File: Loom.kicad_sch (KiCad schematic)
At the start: 49 parts

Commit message: more updates to power distribution
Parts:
- removed FBX1, FBX2: Conn_01x10, symbol Connector_Generic:Conn_01x10
- added FBX1, FBX2: Conn_01x16, symbol Connector_Generic:Conn_01x16
- added PBX1, PBX2: Conn_01x19, symbol Connector_Generic:Conn_01x19
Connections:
- net FPSig: now also PBX2.2 (Pin_2); no longer ECU.8 (Pin_8)
- net FanSig: now also PBX2.4 (Pin_4)
- net GND: now also WSR.8 (Pin_8)
- net MiscPWR: now also FBX1.6 (Pin_6), PBX2.13 (Pin_13); no longer RBX4.85, RBX5.85
- net SENGND: no longer WSR.8 (Pin_8)
- net Shutdown: now also PBX2.1 (Pin_1); no longer LES.2 (Pin_2)
- net SparkCut: now also PBX2.3 (Pin_3)
- net at DBX.1 (Pin_1), DBX.2 (Pin_2), DBX.3 (Pin_3)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: now also FBX2.1 (Pin_1), FBX2.2 (Pin_2), FBX2.3 (Pin_3), FBX2.4 (Pin_4), FBX2.5 (Pin_5), FBX2.6 (Pin_6), FBX2.7 (Pin_7), FBX2.8 (Pin_8)
- net at RBX1.30: now also FBX2.12 (Pin_12), FBX2.13 (Pin_13)
- net at RBX2.30: now also FBX2.14 (Pin_14)
- net at RBX4.30: now also FBX2.15 (Pin_15)
- net at RBX5.30: now also FBX2.16 (Pin_16)
- net FPPWR: no longer names the net of FLP.1 (Pin_1)
- net FanPWR: no longer names the net of FAN1.1 (Pin_1), FAN2.1 (Pin_1)
- net QSPWR renamed QS_12V
- net SPKPWR renamed SpkPwr
- new net: LES.2 (Pin_2), PBX1.1 (Pin_1)
- new net BrakeLightPwr: FBX1.7 (Pin_7), PBX2.15 (Pin_15)
- new net ECUPwr: FBX1.1 (Pin_1), PBX2.5 (Pin_5)
- new net ETCCUPwr: FBX1.3 (Pin_3), PBX2.7 (Pin_7)
- new net ETCStepPwr: FBX1.4 (Pin_4), PBX2.9 (Pin_9)
- new net FPPwr: FBX1.14 (Pin_14), PBX2.10 (Pin_10)
- new net FanPwr: FBX1.16 (Pin_16), PBX2.14 (Pin_14)
- new net INJAPwr: FBX1.12 (Pin_12), PBX2.17 (Pin_17)
- new net INJBPwr: FBX1.13 (Pin_13), PBX2.19 (Pin_19)
- new net LambdaPwr: FBX1.2 (Pin_2), PBX2.6 (Pin_6)
- new net MiscPwr: FBX1.8 (Pin_8), PBX2.8 (Pin_8)
- new net ShutdownPwr: FBX1.5 (Pin_5), PBX2.11 (Pin_11), RBX4.85, RBX5.85
- new net SparkPwr: FBX1.15 (Pin_15), PBX2.12 (Pin_12)
- no-connect marks 10 -> 19
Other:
- sheet Front of Firewall ports: added Brake Light Power, ETC CU Power, Shutdown Power; removed none
- note added: "ECU 2A Lambda 5A ETC CU 5A ETC Stepper 5A Shutdown 5A QS CU 5A Brake Light 5A Misc 10A INJA 5A INJB 5A FP 10A Spark 20A Fans 20A"
- note added: "FIREWALL CONNECTOR HDP24-24-31SE Pinout: 1 MiscPWR 2 ETC CU Power 3 StepperPWR 4 IdleCtrl 5 Blip 6 TPS Power 1 7 TPS Signal 1 8 TPS Ground 1 9 TPS Power 2 10 TPS Signal 2 11 TPS Ground 2 12 Stepper 1+ 13 Stepper 1- 14 Stepper 2+ 15 Stepper 2- 16 Neutral 17 Shift Down 18 Shift Up 19 Tachometer 20 Shutdown Out 21 Starter Sig 22 Fan Sig 23 BLS Sig 24 Launch Sig 25 Launch LED 26 27 28 Brake Light PWR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"
- note added: "Red - up to 15A each Green - up to 20A each"
- note removed: "ECU 2A Lambda 5A ETC CU 5A ETC Stepper 5A Shutdown Circuit 5A QS CU 5A Brake Light 5A Supplemental Electronics 10A INJA 5A INJB 5A FP 10A Spark 20A Fans 20A"
- note removed: "FIREWALL CONNECTOR HDP24-24-31SE Pinout: 1 MiscPWR 2 StepperPWR 3 4 IdleCtrl 5 Blip 6 TPS Power 1 7 TPS Signal 1 8 TPS Ground 1 9 TPS Power 2 10 TPS Signal 2 11 TPS Ground 2 12 Stepper 1+ 13 Stepper 1- 14 Stepper 2+ 15 Stepper 2- 16 Neutral 17 Shift Down 18 Shift Up 19 Tachometer 20 Shutdown Out 21 Starter Sig 22 Fan Sig 23 BLS Sig 24 Launch Sig 25 Launch LED 26 27 28 29 CANH 30 CANL 31 SENGND"
- moved on the sheet: FAN1, FAN2

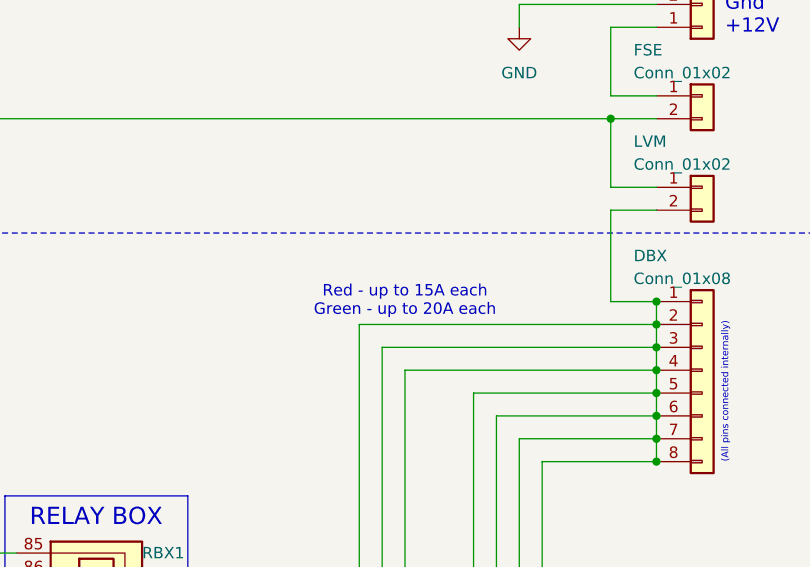
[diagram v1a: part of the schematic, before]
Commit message: More power distribution updates
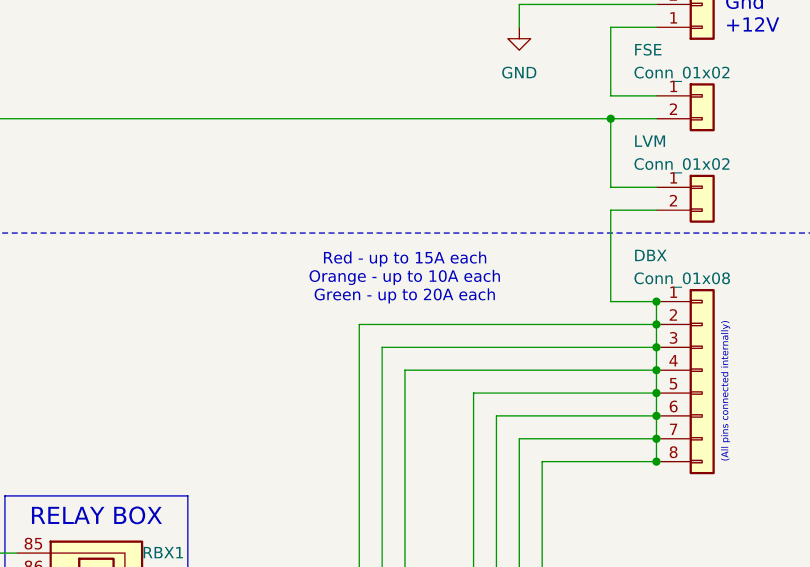
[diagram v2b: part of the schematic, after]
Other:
- note added: "Red - up to 15A each Orange - up to 10A each Green - up to 20A each"
- note removed: "Red - up to 15A each Green - up to 20A each"
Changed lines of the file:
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@@
 		)
 	)
-	(text "Red - up to 15A each\nGreen - up to 20A each"
+	(text "Red - up to 15A each\nOrange - up to 10A each\nGreen - up to 20A each"
 		(exclude_from_sim no)
-		(at 530.86 160.02 0)
+		(at 530.86 157.48 0)
 		(effects
 			(font
@@
 		(at 474.98 284.48)
 		(diameter 0)
-		(color 0 0 0 0)
+		(color 0 255 0 1)
 	)
 	(junction
@@
 		(at 485.14 251.46)
 		(diameter 0)
-		(color 0 0 0 0)
+		(color 0 255 0 1)
 	)
 	(junction
@@
 			(width 0)
 			(type default)
+			(color 0 255 0 1)
 		)
 	)
@@
 			(width 0)
 			(type default)
+			(color 0 255 0 1)
 		)
 	)
@@
 			(width 0)
 			(type default)
+			(color 226 113 0 1)
 		)
 	)
@@
 			(width 0)
 			(type default)
+			(color 0 255 0 1)
 		)
 	)
@@
 			(width 0)
 			(type default)
+			(color 0 255 0 1)
 		)
 	)
@@
 			(width 0)
 			(type default)
+			(color 0 255 0 1)
 		)
 	)
@@
 			(width 0)
 			(type default)
+			(color 0 255 0 1)
 		)
 	)
@@
 			(width 0)
 			(type default)
-			(color 255 0 0 1)
+			(color 0 255 0 1)
 		)
 	)
@@
 			(width 0)
 			(type default)
+			(color 226 113 0 1)
 		)
 	)
@@
 			(width 0)
 			(type default)
+			(color 0 255 0 1)
 		)
 	)
@@
 			(width 0)
 			(type default)
+			(color 0 255 0 1)
 		)
 	)
@@
 			(width 0)
 			(type default)
+			(color 0 255 0 1)
 		)
 	)
@@
 			(width 0)
 			(type default)
+			(color 0 255 0 1)
 		)
 	)
@@
 			(width 0)
 			(type default)
+			(color 226 113 0 1)
 		)
 	)
@@
 			(width 0)
 			(type default)
+			(color 226 113 0 1)
 		)
 	)
@@
 			(width 0)
 			(type default)
+			(color 0 255 0 1)
 		)
 	)
@@
 			(width 0)
 			(type default)
+			(color 0 255 0 1)
 		)
 	)
@@
 			(width 0)
 			(type default)
+			(color 0 255 0 1)
 		)
 	)
@@
 			(width 0)
 			(type default)
+			(color 0 255 0 1)
 		)
 	)
@@
 			(width 0)
 			(type default)
+			(color 0 255 0 1)
 		)
 	)
@@
 			(width 0)
 			(type default)
+			(color 0 255 0 1)
 		)
 	)
@@
 			(width 0)
 			(type default)
+			(color 0 255 0 1)
 		)
 	)
@@
 			(width 0)
 			(type default)
-			(color 255 0 0 1)
+			(color 0 255 0 1)
 		)
 	)
@@
 			(width 0)
 			(type default)
+			(color 0 255 0 1)
 		)
 	)
@@
 			(width 0)
 			(type default)
+			(color 0 255 0 1)
 		)
 	)
@@
 			(width 0)
 			(type default)
+			(color 0 255 0 1)
 		)
 	)
@@
 			(width 0)
 			(type default)
+			(color 0 255 0 1)
 		)
 	)
@@
 			(width 0)
 			(type default)
+			(color 0 255 0 1)
 		)
 	)
@@
 			(width 0)
 			(type default)
+			(color 0 255 0 1)
 		)
 	)
@@
 			(width 0)
 			(type default)
+			(color 0 255 0 1)
 		)
 	)
@@
 			(width 0)
 			(type default)
-			(color 255 0 0 1)
+			(color 0 255 0 1)
 		)
 	)
@@
 			(width 0)
 			(type default)
+			(color 0 255 0 1)
 		)
 	)
@@
 			(width 0)
 			(type default)
+			(color 226 113 0 1)
 		)
 	)
@@
 			(width 0)
 			(type default)
+			(color 0 255 0 1)
 		)
 	)
@@
 			(width 0)
 			(type default)
+			(color 0 255 0 1)
 		)
 	)
@@
 			(width 0)
 			(type default)
+			(color 0 255 0 1)
 		)
 	)
@@
 			(width 0)
 			(type default)
+			(color 226 113 0 1)
 		)
 	)
@@
 			(width 0)
 			(type default)
+			(color 0 255 0 1)
 		)
 	)
@@
 			(width 0)
 			(type default)
+			(color 0 255 0 1)
 		)
 	)
@@
 			(width 0)
 			(type default)
-			(color 255 0 0 1)
+			(color 0 255 0 1)
 		)
 	)
@@
 			(width 0)
 			(type default)
+			(color 0 255 0 1)
 		)
 	)
@@
 			(width 0)
 			(type default)
+			(color 0 255 0 1)
 		)
 	)
@@
 			(width 0)
 			(type default)
+			(color 0 255 0 1)
 		)
 	)

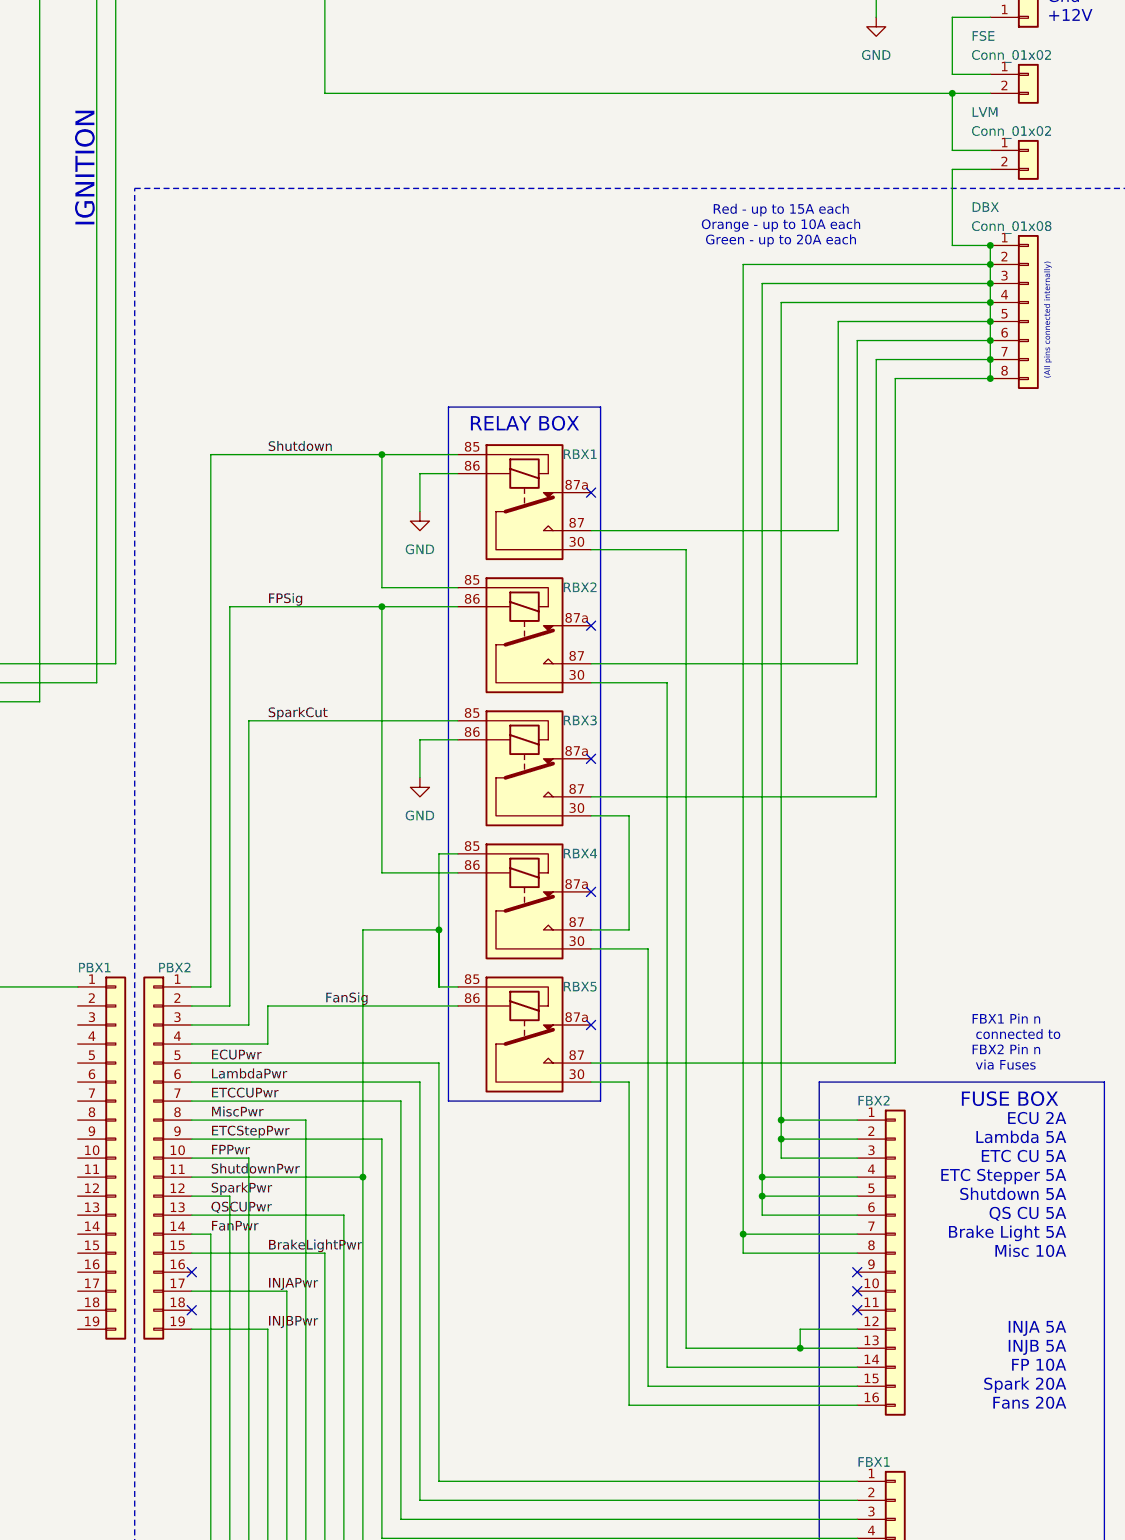
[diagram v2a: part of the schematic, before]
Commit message: Power Box Changes 20250714
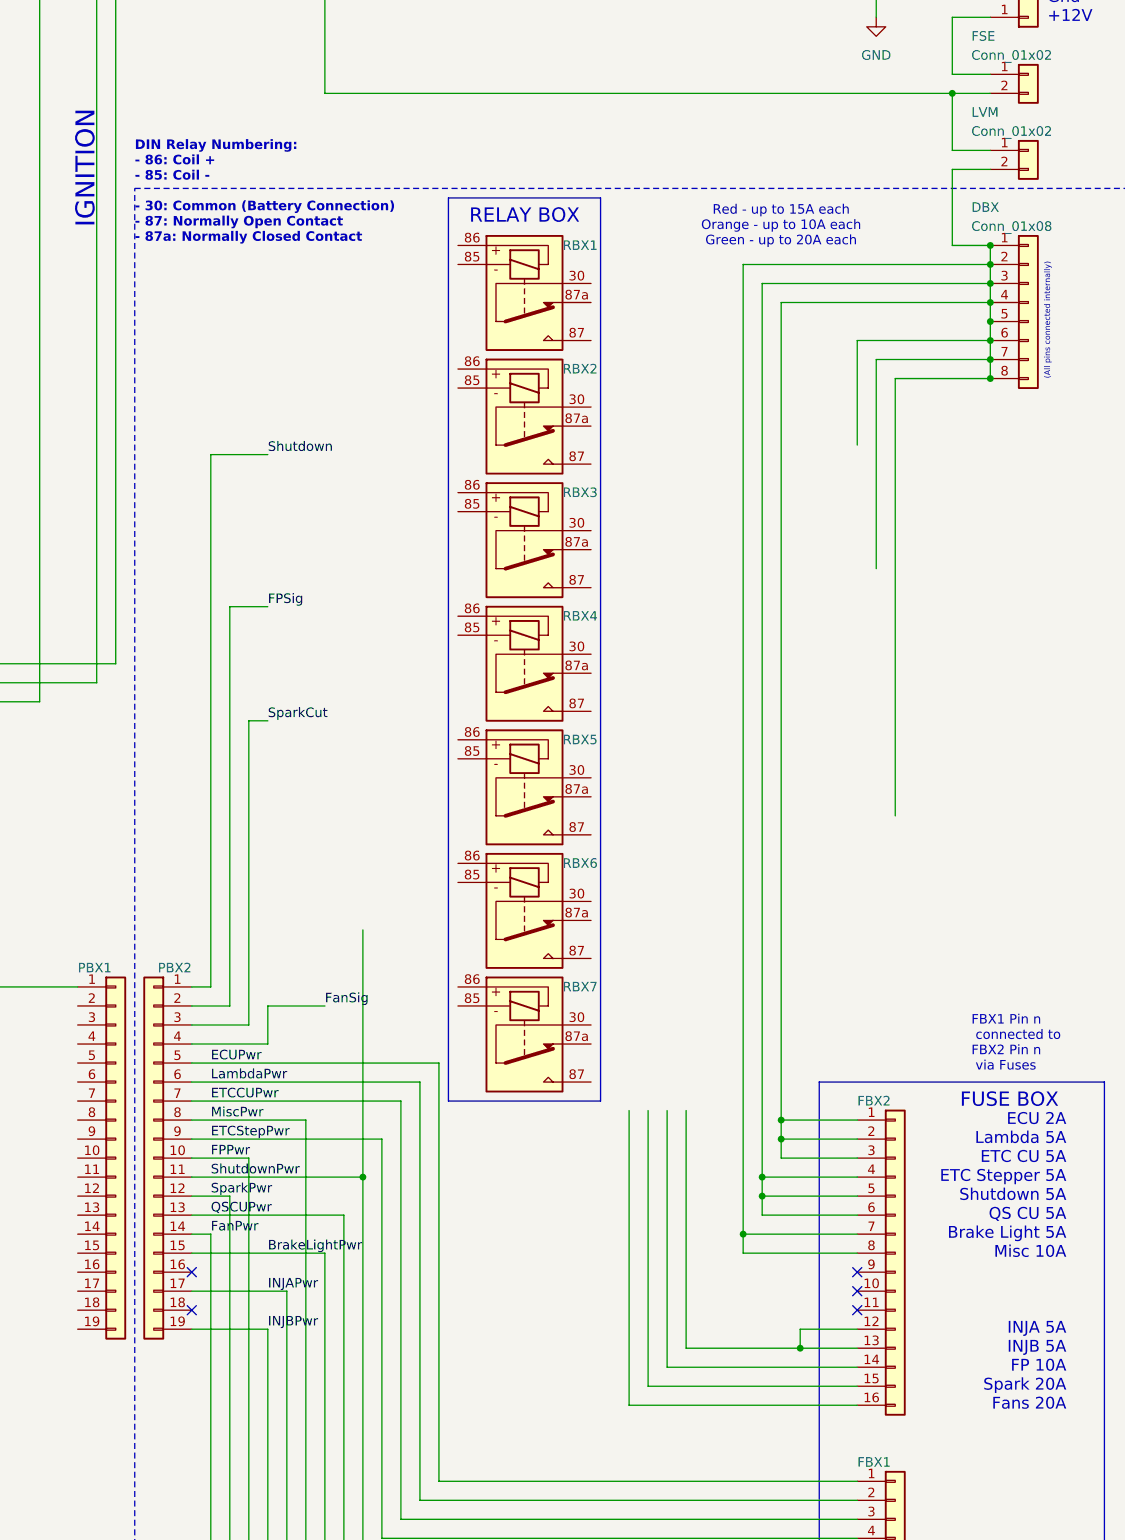
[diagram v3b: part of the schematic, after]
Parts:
- added RBX6, RBX7: Relay_SPDT_Automotive, symbol FBR_Symbols:Relay_SPDT_Automotive
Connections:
- net FPSig: no longer RBX2.86, RBX4.86
- net FanSig: no longer RBX5.86
- net GND: no longer RBX1.86, RBX3.86
- net Shutdown: no longer RBX1.85, RBX2.85
- net ShutdownPwr: no longer RBX4.85, RBX5.85
- net SparkCut: no longer RBX3.85
- net at DBX.1 (Pin_1), DBX.2 (Pin_2), DBX.3 (Pin_3)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: no longer RBX1.87, RBX2.87, RBX3.87, RBX5.87
- net at RBX3.30: no longer RBX4.87
- net at FBX2.12 (Pin_12), FBX2.13 (Pin_13): no longer RBX1.30
- net at RBX2.30: no longer FBX2.14 (Pin_14)
- net at RBX4.30: no longer FBX2.15 (Pin_15)
- net at RBX5.30: no longer FBX2.16 (Pin_16)
- no-connect marks 19 -> 14
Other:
- note added: "DIN Relay Numbering: - 86: Coil + - 85: Coil - - 30: Common (Battery Connection) - 87: Normally Open Contact - 87a: Normally Closed Contact"
